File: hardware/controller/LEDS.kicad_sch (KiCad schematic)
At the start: 17 parts, among them IC1 PCA9685PW_Q900,118

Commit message: asdasd
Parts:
- added LED5: LO_M676-Q2S1-24-Z, LEDM2214X140N, symbol Device:LED
- added R19: 150R, RESC2012X60N, symbol Device:R
- renumbered IC1 to IC2, LED2 to LED1, LED3 to LED2, LED4 to LED3, LED5 to LED4, R2 to R11, R5 to R12, R8 to R13, R11 to R14, R3 to R15, R6 to R16, R9 to R17, R12 to R18, R1 to R7, R4 to R8, R7 to R9
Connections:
- net C_BLU1: now also IC2.15 (LED8); no longer IC2.16 (LED9)
- net C_BLU2: now also IC2.16 (LED9); no longer IC2.17 (LED10)
- net C_BLU3: now also IC2.17 (LED10); no longer IC2.18 (LED11)
- net C_BLU4: now also IC2.18 (LED11); no longer IC2.19 (LED12)
- net GND: now also R19.1
- new net: LED5.1 (K), R19.2
- new net +3V3: LED5.2 (A)
- no-connect marks 0 -> 4
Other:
- note added: "todo: find bigger RGB leds"

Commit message: a
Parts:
- added R20: 10kR, symbol Device:R
- added R21, R22: 3R3k, symbol Device:R
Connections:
- net +5V is gone; now on net +3V3: IC2.28 (VDD), LED1.4 (ANODE), LED2.4 (ANODE), LED3.4 (ANODE), LED4.4 (ANODE)
- net +3V3: now also IC2.1 (A0), IC2.2 (A1), IC2.3 (A2), IC2.4 (A3), IC2.5 (A4), R21.1, R22.1
- net GND: now also R20.1
- net SCL: now also R22.2
- net SDA: now also R21.2
- net ~{OE}: now reaches IC2.23 (~{OE})
- net ~{OE}: now also R20.2
- no-connect marks 4 -> 6
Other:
- note added: "I2C Addy: 1 1 1 1 1 0 = #62 = 0x3E"

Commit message: fixed bus stuff
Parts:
- removed LED1, LED2, LED3, LED4: UHD111A-FKA-C3K23E1L3VG5ZB3Z3, UHD111AFKAC3K23E1L3VG5ZB3Z3, symbol SamacSys_Parts:UHD111A-FKA-C3K23E1L3VG5ZB3Z3
- added LED1, LED2, LED3, LED4: SM0605RGB, SM0605RGB, symbol SamacSys_Parts:SM0605RGB
- added LED6: LO_M676-Q2S1-24-Z, LEDM2214X140N, symbol Device:LED
- added R31: 150R, RESC2012X60N, symbol Device:R
- renumbered R21 to R15, R20 to R16, R22 to R17, R7 to R18, R8 to R19, R9 to R20, R10 to R21, R11 to R22, R12 to R23, R13 to R24, R14 to R25, R15 to R26, R16 to R27, R17 to R28, R18 to R29, R19 to R30
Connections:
- net +3V3: now also LED1.1 (ANODE), LED2.1 (ANODE), LED3.1 (ANODE), LED4.1 (ANODE)
- net GND: now also R31.1
- net at R25.1: now also LED4.4 (C_GREEN)
- net at R26.1: now also LED1.2 (C_BLUE)
- net at R22.1: now also LED1.4 (C_GREEN)
- net at R18.1: now also LED1.3 (C_RED)
- net at R29.1: now also LED4.2 (C_BLUE)
- net at R21.1: now also LED4.3 (C_RED)
- net at R28.1: now also LED3.2 (C_BLUE)
- net at R19.1: now also LED2.3 (C_RED)
- net at R24.1: now also LED3.4 (C_GREEN)
- net at R20.1: now also LED3.3 (C_RED)
- net at R27.1: now also LED2.2 (C_BLUE)
- net at R23.1: now also LED2.4 (C_GREEN)
- new net: LED6.1 (K), R31.2
- new net GPIO: LED6.2 (A)
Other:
- note added: "GPIO Runtime LED"
- note added: "LED Driver"
- note added: "Power LED"
- note added: "RGB LEDs"
- note removed: "todo: find bigger RGB leds"
- moved on the sheet: IC2, LED5, R15, R16, R17, R18, R19, R20, R21, R22, R23, R24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

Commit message: added memory and fixed gpio pins
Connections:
- net GPIO renamed LED GPIO
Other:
- moved on the sheet: LED6, R31
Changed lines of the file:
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@@
 	(rectangle
 		(start 209.55 80.01)
-		(end 242.57 111.76)
+		(end 247.65 111.76)
 		(stroke
 			(width 0)
@@
 	)
 	(bus_entry
+		(at 44.45 29.21)
+		(size 2.54 2.54)
+		(stroke
+			(width 0)
+			(type default)
+		)
+	)
+	(bus_entry
 		(at 44.45 24.13)
 		(size 2.54 2.54)
@@
 	(wire
 		(pts
+			(xy 44.45 35.56) (xy 53.34 35.56)
+		)
+		(stroke
+			(width 0)
+			(type default)
+		)
+	)
+	(wire
+		(pts
 			(xy 193.04 59.69) (xy 167.64 59.69)
 		)
@@
 		)
 	)
+	(bus
+		(pts
+			(xy 44.45 26.67) (xy 44.45 29.21)
+		)
+		(stroke
+			(width 0)
+			(type default)
+		)
+	)
 	(wire
 		(pts
@@
 	(wire
 		(pts
-			(xy 217.17 85.09) (xy 217.17 87.63)
+			(xy 46.99 31.75) (xy 52.07 31.75)
+		)
+		(stroke
+			(width 0)
+			(type default)
+		)
+	)
+	(wire
+		(pts
+			(xy 222.25 85.09) (xy 222.25 87.63)
 		)
 		(stroke
@@
 		)
 	)
+	(label "LED_GPIO"
+		(at 222.25 85.09 180)
+		(effects
+			(font
+				(size 1.27 1.27)
+			)
+			(justify right bottom)
+		)
+	)
 	(label "C_BLU3"
 		(at 99.06 87.63 0)
@@
 	)
 	(label "~{OE}"
+		(at 52.07 31.75 180)
+		(effects
+			(font
+				(size 1.27 1.27)
+			)
+			(justify right bottom)
+		)
+	)
+	(label "~{OE}"
 		(at 116.84 72.39 0)
 		(effects
@@
 		)
 	)
+	(label "LED_GPIO"
+		(at 53.34 35.56 180)
+		(effects
+			(font
+				(size 1.27 1.27)
+			)
+			(justify right bottom)
+		)
+	)
 	(label "C_BLU4"
 		(at 99.06 85.09 0)
@@
 		)
 	)
-	(hierarchical_label "GPIO"
+	(hierarchical_label "LED GPIO"
 		(shape input)
-		(at 217.17 85.09 180)
+		(at 44.45 35.56 180)
 		(effects
 			(font
@@
 	(symbol
 		(lib_id "power:GND")
-		(at 217.17 102.87 0)
+		(at 222.25 102.87 0)
 		(unit 1)
 		(exclude_from_sim no)
@@
 		(fields_autoplaced yes)
 		(property "Reference" "#PWR052"
-			(at 217.17 109.22 0)
+			(at 222.25 109.22 0)
 			(effects
 				(font
@@
 		)
 		(property "Value" "GND"
-			(at 217.17 107.95 0)
+			(at 222.25 107.95 0)
 			(effects
 				(font
@@
 		)
 		(property "Footprint" ""
-			(at 217.17 102.87 0)
+			(at 222.25 102.87 0)
 			(effects
 				(font
@@
 		)
 		(property "Datasheet" ""
-			(at 217.17 102.87 0)
+			(at 222.25 102.87 0)
 			(effects
 				(font
@@
 		)
 		(property "Description" "Power symbol creates a global label with name \"GND\" , ground"
-			(at 217.17 102.87 0)
+			(at 222.25 102.87 0)
 			(effects
 				(font
@@
 	(symbol
 		(lib_id "Device:LED")
-		(at 217.17 91.44 90)
+		(at 222.25 91.44 90)
 		(unit 1)
 		(exclude_from_sim no)
@@
 		(dnp no)
 		(property "Reference" "LED6"
-			(at 219.964 91.694 90)
+			(at 225.044 91.694 90)
 			(effects
 				(font
@@
 		)
 		(property "Value" "LO_M676-Q2S1-24-Z"
-			(at 219.964 94.234 90)
+			(at 225.044 94.234 90)
 			(effects
 				(font
@@
 		)
 		(property "Footprint" "LEDM2214X140N"
-			(at 217.17 91.44 0)
+			(at 222.25 91.44 0)
 			(effects
 				(font
@@
 		)
 		(property "Datasheet" "~"
-			(at 217.17 91.44 0)
+			(at 222.25 91.44 0)
 			(effects
 				(font
@@
 		)
 		(property "Description" "Light emitting diode"
-			(at 217.17 91.44 0)
+			(at 222.25 91.44 0)
 			(effects
 				(font
@@
 		)
 		(property "Height" "1.4"
-			(at 610.82 78.74 0)
+			(at 615.9 78.74 0)
 			(effects
 				(font
@@
 		)
 		(property "Mouser Part Number" "720-LOM676Q2S124Z"
-			(at 710.82 78.74 0)
+			(at 715.9 78.74 0)
 			(effects
 				(font
@@
 		)
 		(property "Mouser Price/Stock" "https://www.mouser.co.uk/ProductDetail/OSRAM-Opto-Semiconductors/LO-M676-Q2S1-24-Z?qs=nTDll3UaDK6JlNmxoQCpEQ%3D%3D"
-			(at 810.82 78.74 0)
+			(at 815.9 78.74 0)
 			(effects
 				(font
@@
 		)
 		(property "Manufacturer_Name" "ams OSRAM"
-			(at 910.82 78.74 0)
+			(at 915.9 78.74 0)
 			(effects
 				(font
@@
 		)
 		(property "Manufacturer_Part_Number" "LO M676-Q2S1-24-Z"
-			(at 1010.82 78.74 0)
+			(at 1015.9 78.74 0)
 			(effects
 				(font
@@
 		)
 		(property "Sim.Pins" "1=K 2=A"
-			(at 217.17 91.44 0)
+			(at 222.25 91.44 0)
 			(effects
 				(font
@@
 	(symbol
 		(lib_id "Device:R")
-		(at 217.17 99.06 180)
+		(at 222.25 99.06 180)
 		(unit 1)
 		(exclude_from_sim no)
@@
 		(dnp no)
 		(property "Reference" "R31"
-			(at 225.552 99.06 0)
+			(at 230.632 99.06 0)
 			(effects
 				(font
@@
 		)
 		(property "Value" "150R"
-			(at 220.98 99.06 0)
+			(at 226.06 99.06 0)
 			(effects
 				(font
@@
 		)
 		(property "Footprint" "RESC2012X60N"
-			(at 218.948 99.06 90)
+			(at 224.028 99.06 90)
 			(effects
 				(font
@@
 		)
 		(property "Datasheet" "~"
-			(at 217.17 99.06 0)
+			(at 222.25 99.06 0)
 			(effects
 				(font
@@
 		)
 		(property "Description" "Resistor"
-			(at 217.17 99.06 0)
+			(at 222.25 99.06 0)
 			(effects
 				(font
@@
 		)
 		(property "Manufacturer_Name" "KOA Speer"
-			(at 217.17 99.06 90)
+			(at 222.25 99.06 90)
 			(effects
 				(font
@@
 		)
 		(property "Manufacturer_Part_Number" "RK73B2ATTD151J"
-			(at 217.17 99.06 90)
+			(at 222.25 99.06 90)
 			(effects
 				(font
@@
 		)
 		(property "Mouser Part Number" "660-RK73B2ATTD151J"
-			(at 217.17 99.06 90)
+			(at 222.25 99.06 90)
 			(effects
 				(font
@@
 		)
 		(property "Mouser Price/Stock" "https://www.mouser.co.uk/ProductDetail/KOA-Speer/RK73B2ATTD151J?qs=Eg3swSo9kV1ngoeZFqQs4w%3D%3D"
-			(at 217.17 99.06 90)
+			(at 222.25 99.06 90)
 			(effects
 				(font

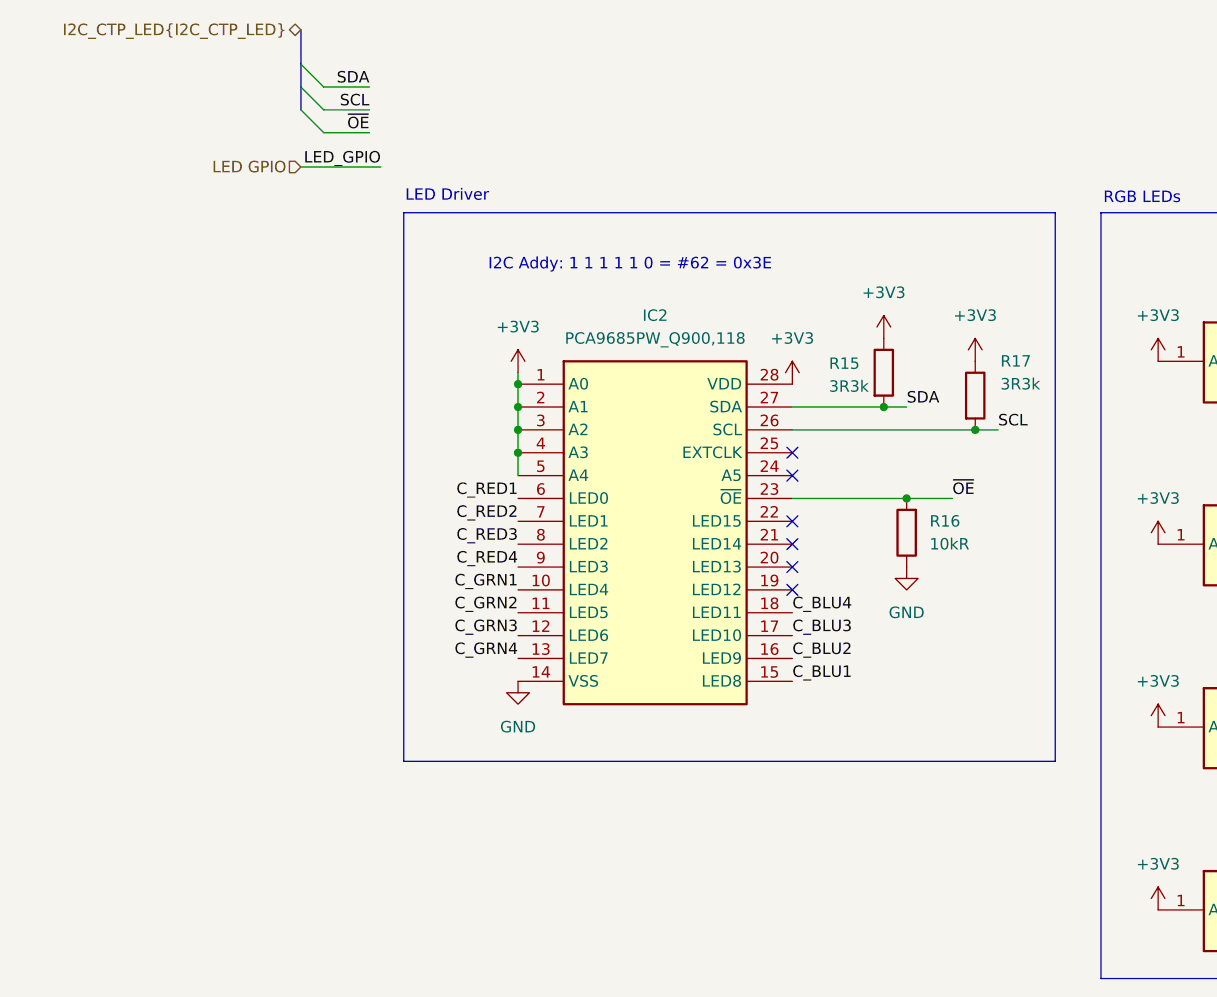
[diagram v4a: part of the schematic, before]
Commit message: modified power circuitry
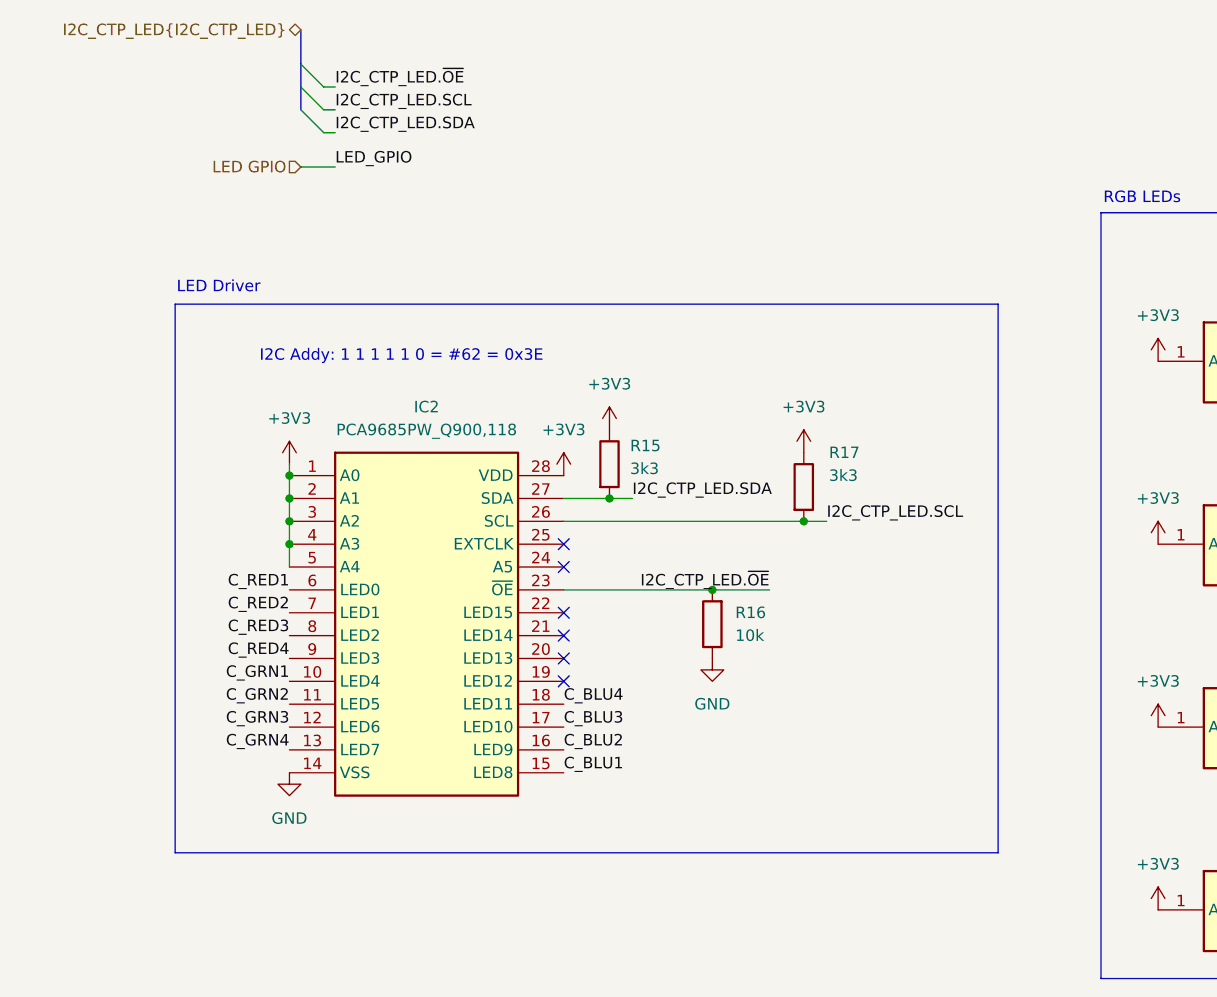
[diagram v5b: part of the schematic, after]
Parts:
- IC2: footprint SOP65P640X110-28N -> SamacSys_Parts:SOP65P640X110-28N
- LED1, LED2, LED3, LED4: footprint SM0605RGB -> SamacSys_Parts:SM0605RGB
- LED5, LED6: footprint LEDM2214X140N -> SamacSys_Parts:LEDM2214X140N
- R15, R17: value 3R3k -> 3k3
- R16: value 10kR -> 10k
- R18, R19, R20, R21, R30, R31: footprint RESC2012X60N -> SamacSys_Parts:RESC2012X60N
- R22, R23, R24, R25, R26, R27, R28, R29: footprint RESC2012X65N -> SamacSys_Parts:RESC2012X65N
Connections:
- net SCL renamed I2C_CTP_LED.SCL
- net SDA renamed I2C_CTP_LED.SDA
- net ~{OE} renamed I2C_CTP_LED.~{OE}
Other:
- moved on the sheet: IC2, R15, R16, R17

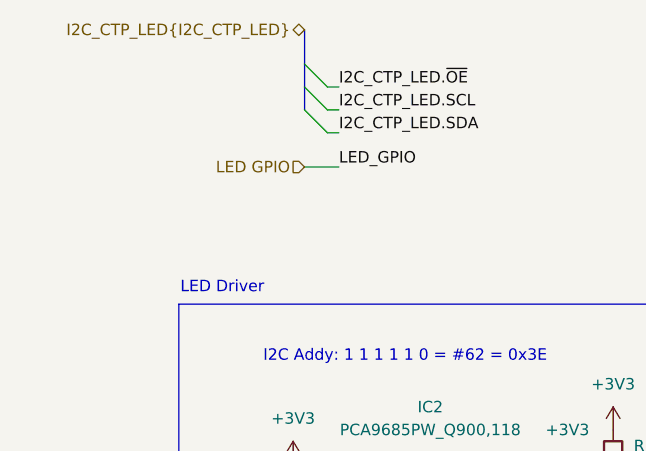
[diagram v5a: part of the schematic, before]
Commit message: finished first rev of controller schematic minus actually finding passive components. moved some features to rev2 todo
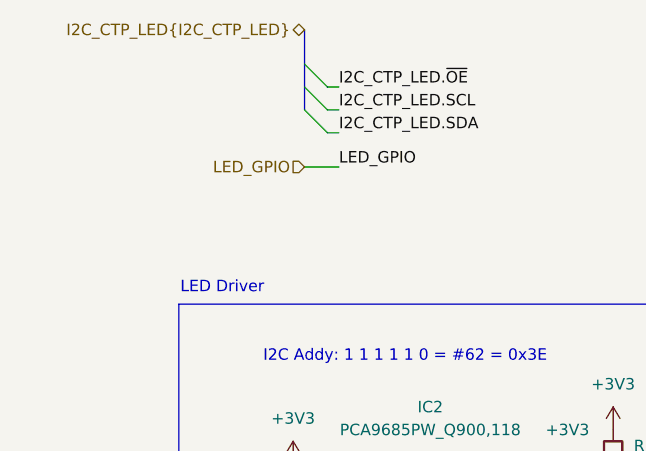
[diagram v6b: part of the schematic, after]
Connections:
- net LED GPIO renamed LED_GPIO
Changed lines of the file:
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@@
 		)
 	)
-	(hierarchical_label "LED GPIO"
+	(hierarchical_label "LED_GPIO"
 		(shape input)
 		(at 44.45 35.56 180)
